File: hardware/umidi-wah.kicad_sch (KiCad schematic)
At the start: 82 parts, among them J1 Conn_01x02, J2 Conn_01x02, J3 Conn_02x05_Odd_Even, J4 Conn_01x02, J5 Input, J6 Output, K1 G6K-2P-Y-DC5, Q1 KSC1815, Q2 KSC1815, Q3 KSC1815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

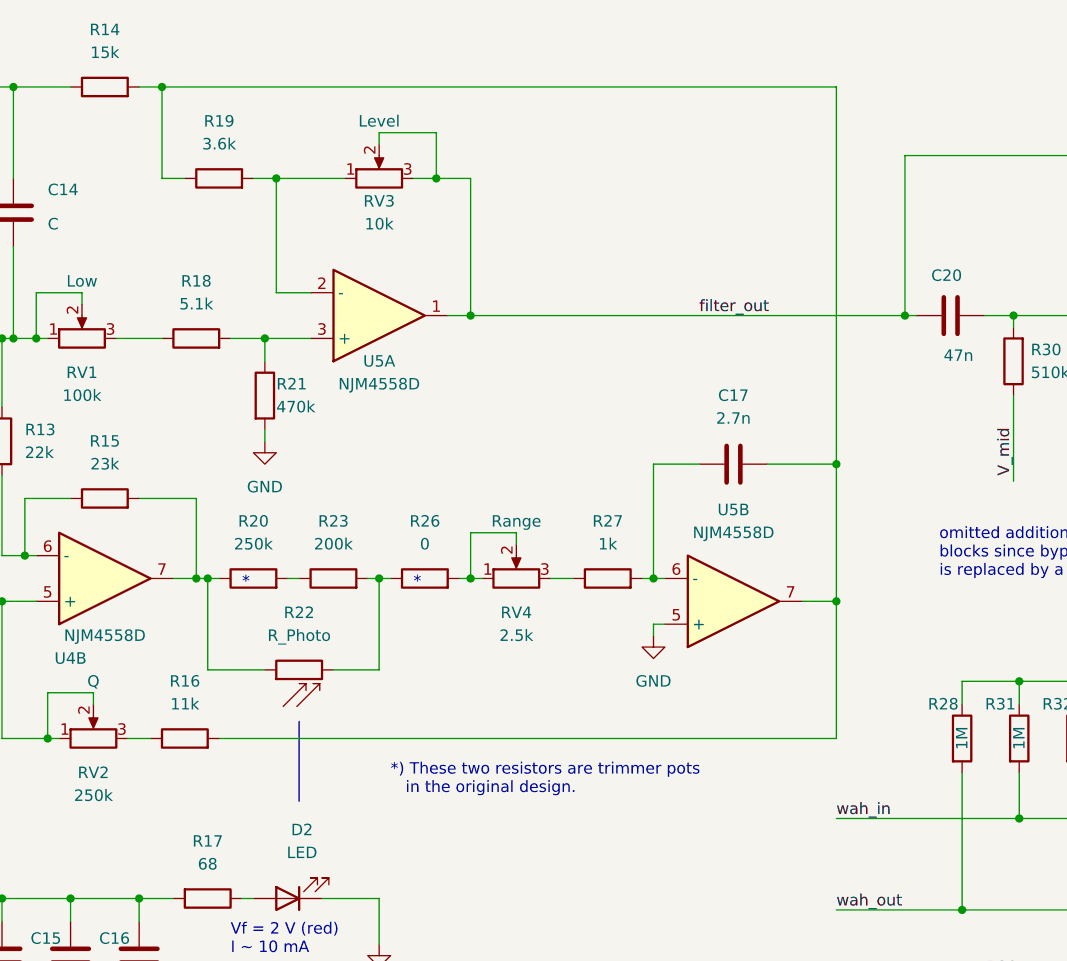
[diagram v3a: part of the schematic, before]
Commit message: Use trim resistors for ldr tuning
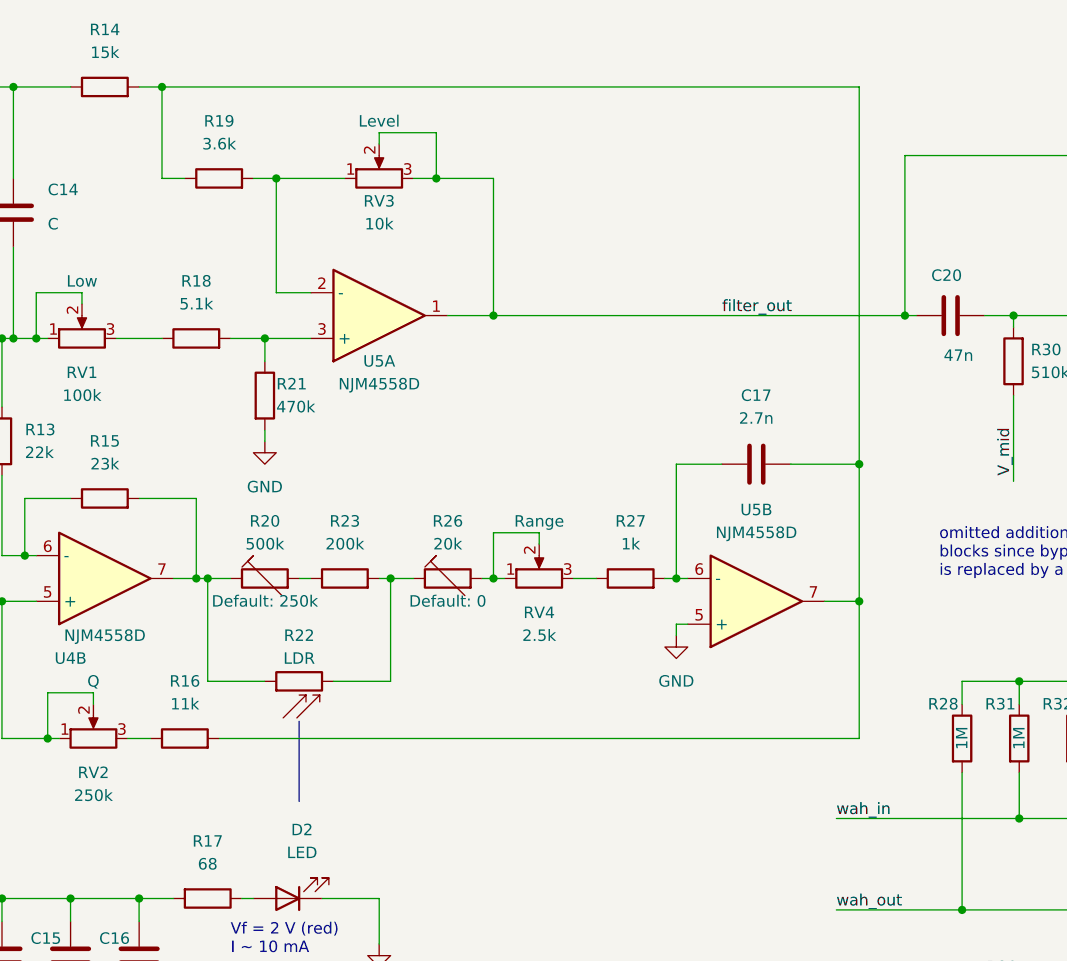
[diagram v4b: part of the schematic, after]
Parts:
- removed R20: 250k, symbol Device:R
- removed R26: 0, symbol Device:R
- added R20: 500k, symbol Device:R_Trim
- added R26: 20k, symbol Device:R_Trim
- R22: value R_Photo -> LDR
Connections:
- net at R15.2, R22.1, U4.7: now also R20.1
- net at R22.2, R23.2: now also R26.1
- net at R23.1: now also R20.2
- net at RV4.1, RV4.2: now also R26.2
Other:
- note removed: "*"
- note removed: "*) These two resistors are trimmer pots in the original design."
- moved on the sheet: C17, R22, R23, R27, RV4, U5B

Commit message: Define trimmer and ldr footprints; Add supply infos
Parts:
- R20: footprint (none) -> Potentiometer_THT:Potentiometer_Piher_PT-10-V10_Vertical_Hole; Manufacturer (none) -> Piher; Manufacturer Part Number (none) -> PT10LV10-504A2020
- R22: footprint (none) -> OptoDevice:R_LDR_4.9x4.2mm_P2.54mm_Vertical; Manufacturer (none) -> Advanced Photonix; Manufacturers Part Number (none) -> PDV P9004 or PDV 9203; Supplier (none) -> Digikey
- R26: footprint (none) -> Potentiometer_THT:Potentiometer_Piher_PT-10-V10_Vertical_Hole; Manufacturer (none) -> Piher; Manufacturer Part Number (none) -> PT10LV10-203A2020
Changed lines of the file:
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@@
       (effects (font (size 1.27 1.27)))
     )
-    (property "Footprint" "" (at 152.4 87.63 90)
+    (property "Footprint" "OptoDevice:R_LDR_4.9x4.2mm_P2.54mm_Vertical" (at 152.4 87.63 90)
       (effects (font (size 1.27 1.27)) (justify left) hide)
     )
@@
       (effects (font (size 1.27 1.27)) hide)
     )
+    (property "Manufacturer" "Advanced Photonix" (at 146.05 88.9 90)
+      (effects (font (size 1.27 1.27)) hide)
+    )
+    (property "Manufacturers Part Number" "PDV P9004 or PDV 9203" (at 146.05 88.9 90)
+      (effects (font (size 1.27 1.27)) hide)
+    )
+    (property "Supplier" "Digikey" (at 146.05 88.9 90)
+      (effects (font (size 1.27 1.27)) hide)
+    )
     (pin "1")
     (pin "2")
@@
       (effects (font (size 1.27 1.27)))
     )
-    (property "Footprint" "" (at 142.24 79.248 90)
+    (property "Footprint" "Potentiometer_THT:Potentiometer_Piher_PT-10-V10_Vertical_Hole" (at 142.24 79.248 90)
       (effects (font (size 1.27 1.27)) hide)
     )
@@
     (property "Default" "250k" (at 142.24 80.01 90) (show_name)
       (effects (font (size 1.27 1.27)))
+    )
+    (property "Manufacturer" "Piher" (at 142.24 77.47 90)
+      (effects (font (size 1.27 1.27)) hide)
+    )
+    (property "Manufacturer Part Number" "  PT10LV10-504A2020" (at 142.24 77.47 90)
+      (effects (font (size 1.27 1.27)) hide)
     )
     (pin "1")
@@
       (effects (font (size 1.27 1.27)))
     )
-    (property "Footprint" "" (at 162.56 79.248 90)
+    (property "Footprint" "Potentiometer_THT:Potentiometer_Piher_PT-10-V10_Vertical_Hole" (at 162.56 79.248 90)
       (effects (font (size 1.27 1.27)) hide)
     )
@@
       (effects (font (size 1.27 1.27)))
     )
-    (pin "1")
+    (property "Manufacturer" "Piher" (at 162.56 77.47 90)
+      (effects (font (size 1.27 1.27)) hide)
+    )
+    (property "Manufacturer Part Number" "PT10LV10-203A2020" (at 162.56 77.47 90)
+      (effects (font (size 1.27 1.27)) hide)
+    )
+    (pin "1")

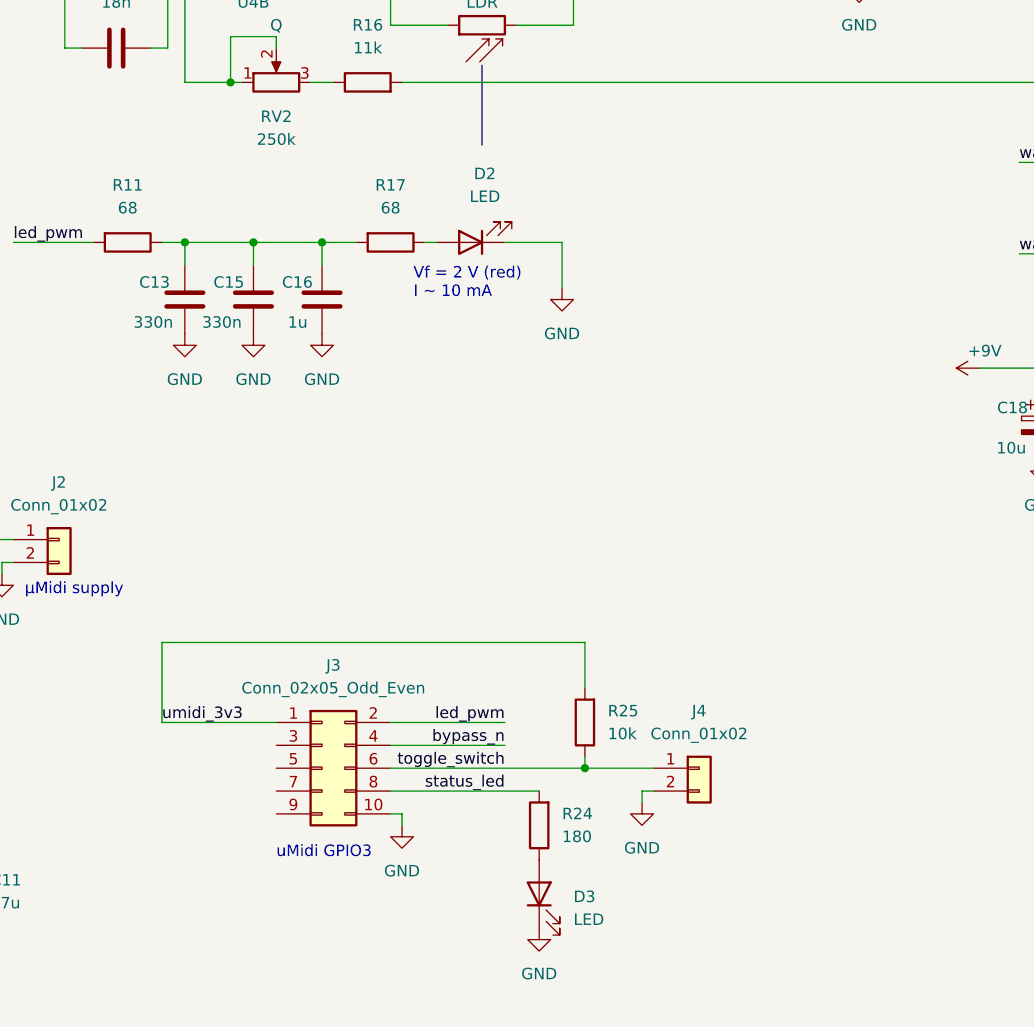
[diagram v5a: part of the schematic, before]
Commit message: Add all uMidi pin sockets for  mech stability
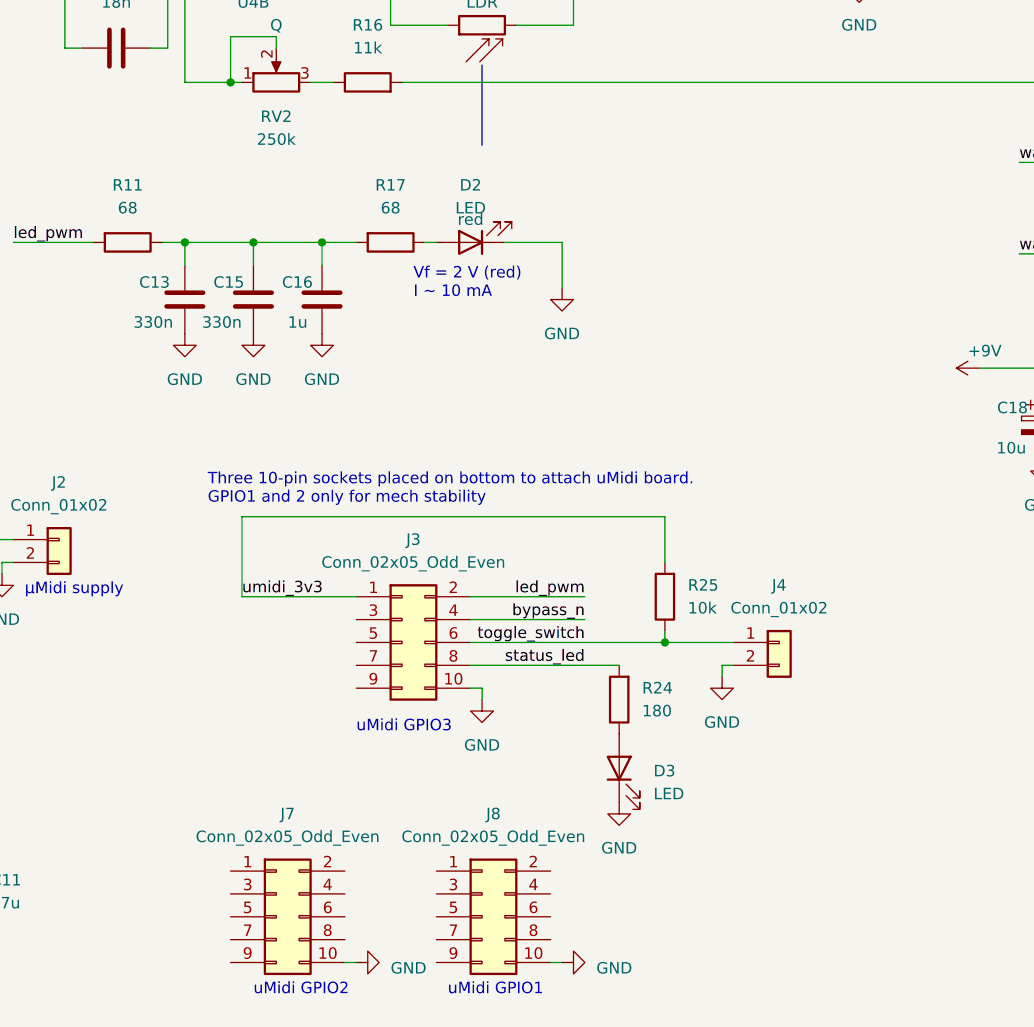
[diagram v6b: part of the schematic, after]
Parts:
- added J7, J8: Conn_02x05_Odd_Even, Connector_PinSocket_2.54mm:PinSocket_2x05_P2.54mm_Vertical, symbol Connector_Generic:Conn_02x05_Odd_Even
- D2: footprint (none) -> LED_THT:LED_D5.0mm; Color (none) -> red
- J3: footprint Connector_IDC:IDC-Header_2x05_P2.54mm_Vertical -> Connector_PinSocket_2.54mm:PinSocket_2x05_P2.54mm_Vertical
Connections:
- net GND: now also J7.10 (Pin_10), J8.10 (Pin_10)
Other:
- note added: "Three 10-pin sockets placed on bottom to attach uMidi board. GPIO1 and 2 only for mech stability"
- note added: "uMidi GPIO1"
- note added: "uMidi GPIO2"
- moved on the sheet: D3, J3, J4, R24, R25

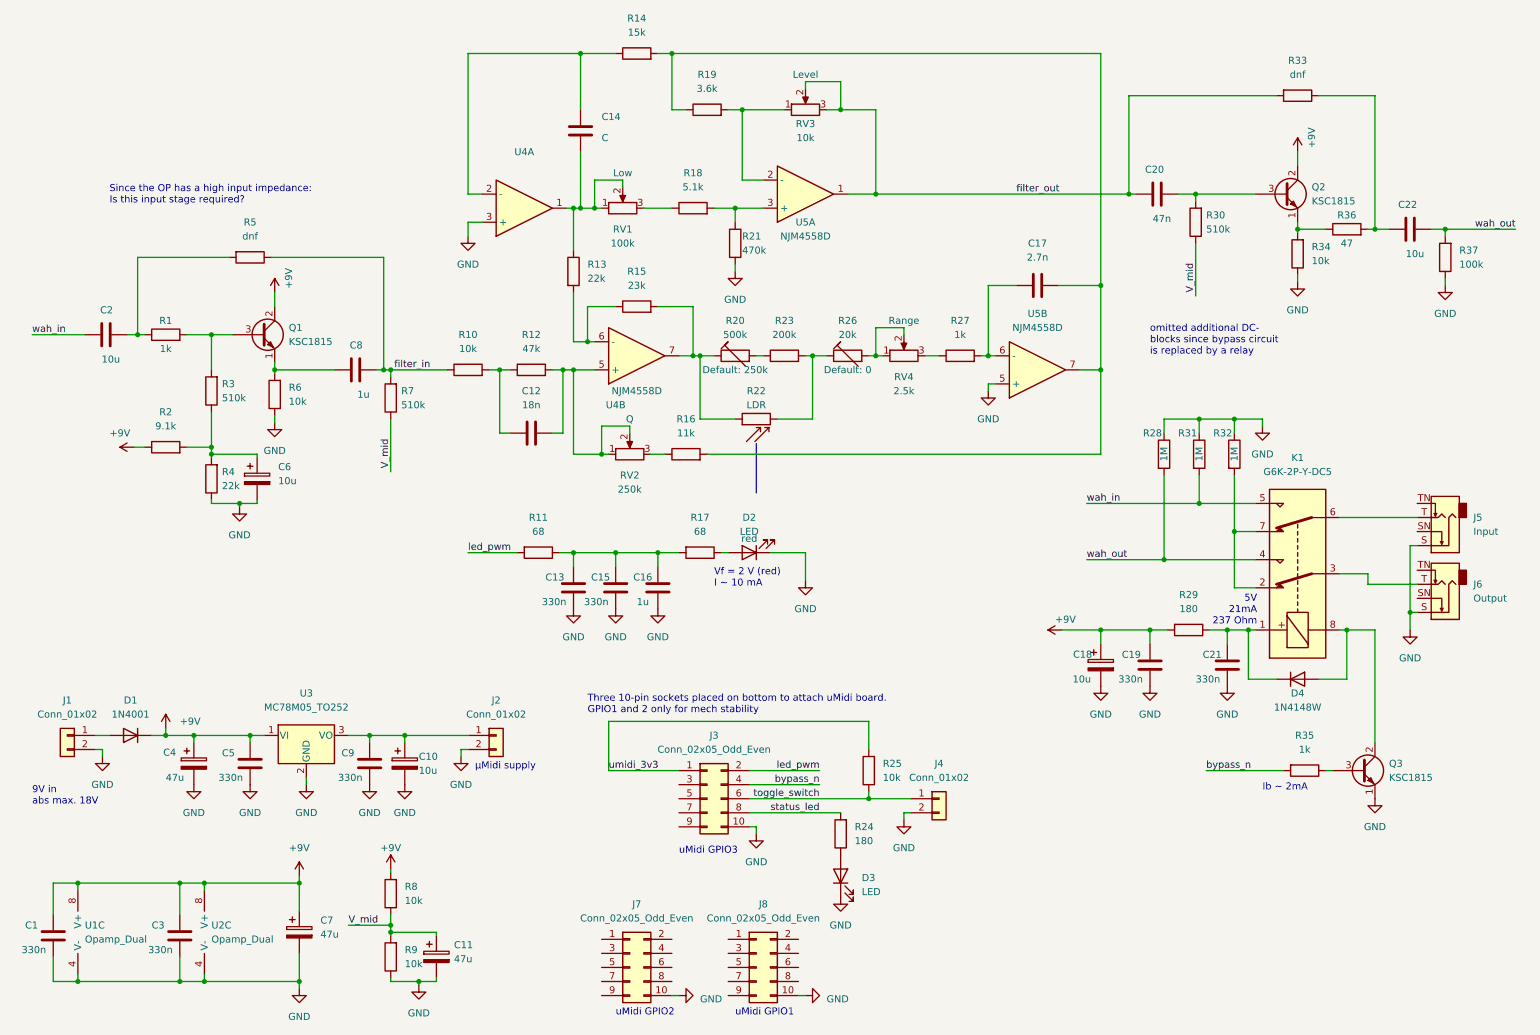
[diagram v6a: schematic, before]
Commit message: Move filter circuit to designated sheet
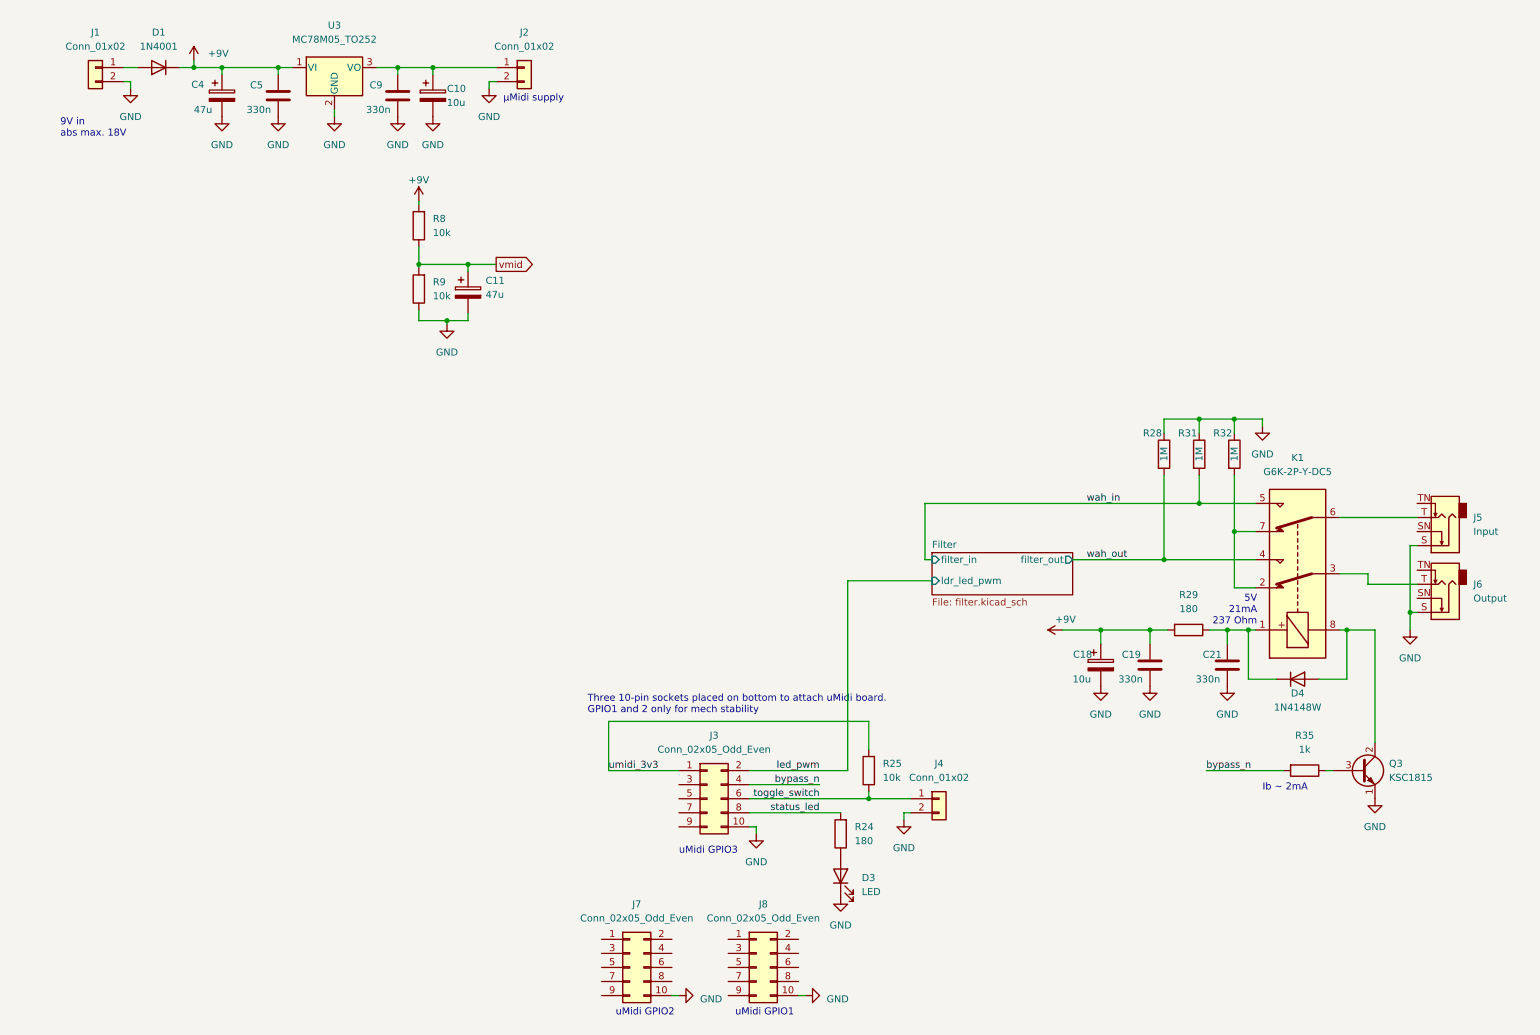
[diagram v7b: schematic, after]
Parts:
- removed C1, C13, C15, C3: 330n, symbol Device:C
- removed C12: 18n, symbol Device:C
- removed C14: C, symbol Device:C
- removed C16, C8: 1u, symbol Device:C
- removed C17: 2.7n, symbol Device:C
- removed C2, C22: 10u, symbol Device:C
- removed C20: 47n, symbol Device:C
- removed C6: 10u, symbol Device:C_Polarized
- removed C7: 47u, symbol Device:C_Polarized
- removed D2: LED, LED_THT:LED_D5.0mm, symbol Device:LED
- removed Q1, Q2: KSC1815, Package_TO_SOT_THT:TO-92, symbol Device:Q_NPN_ECB
- removed R1, R27: 1k, symbol Device:R
- removed R10, R34, R6: 10k, symbol Device:R
- removed R11, R17: 68, symbol Device:R
- removed R12: 47k, symbol Device:R
- removed R13, R4: 22k, symbol Device:R
- removed R14: 15k, symbol Device:R
- removed R15: 23k, symbol Device:R
- removed R16: 11k, symbol Device:R
- removed R18: 5.1k, symbol Device:R
- removed R19: 3.6k, symbol Device:R
- removed R2: 9.1k, symbol Device:R
- removed R20: 500k, Potentiometer_THT:Potentiometer_Piher_PT-10-V10_Vertical_Hole, symbol Device:R_Trim
- removed R21: 470k, symbol Device:R
- removed R22: LDR, OptoDevice:R_LDR_4.9x4.2mm_P2.54mm_Vertical, symbol Device:R_Photo
- removed R23: 200k, symbol Device:R
- removed R26: 20k, Potentiometer_THT:Potentiometer_Piher_PT-10-V10_Vertical_Hole, symbol Device:R_Trim
- removed R3, R30, R7: 510k, symbol Device:R
- removed R33, R5: dnf, symbol Device:R
- removed R36: 47, symbol Device:R
- removed R37: 100k, symbol Device:R
- removed RV1: 100k, symbol Device:R_Potentiometer
- removed RV2: 250k, symbol Device:R_Potentiometer
- removed RV3: 10k, symbol Device:R_Potentiometer
- removed RV4: 2.5k, symbol Device:R_Potentiometer
- removed U1, U2: Opamp_Dual, symbol Device:Opamp_Dual
- removed U4, U5: NJM4558D, Package_DIP:DIP-8_W7.62mm_Socket_LongPads, symbol Device:Opamp_Dual
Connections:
- net V_mid renamed vmid
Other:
- added sheet Filter (filter.kicad_sch)
- note removed: "Since the OP has a high input impedance: Is this input stage required?"
- note removed: "Vf = 2 V (red) I ~ 10 mA"
- note removed: "omitted additional DC- blocks since bypass circuit is replaced by a relay"
- moved on the sheet: C10, C11, C4, C5, C9, D1, J1, J2, R8, R9, U3
